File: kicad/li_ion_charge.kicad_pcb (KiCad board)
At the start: 2 copper layers, 17 parts, among them P101 USB_A, P102 CONN_01X02, P103 CONN_01X02, U101 MCP73834-FCI/UN

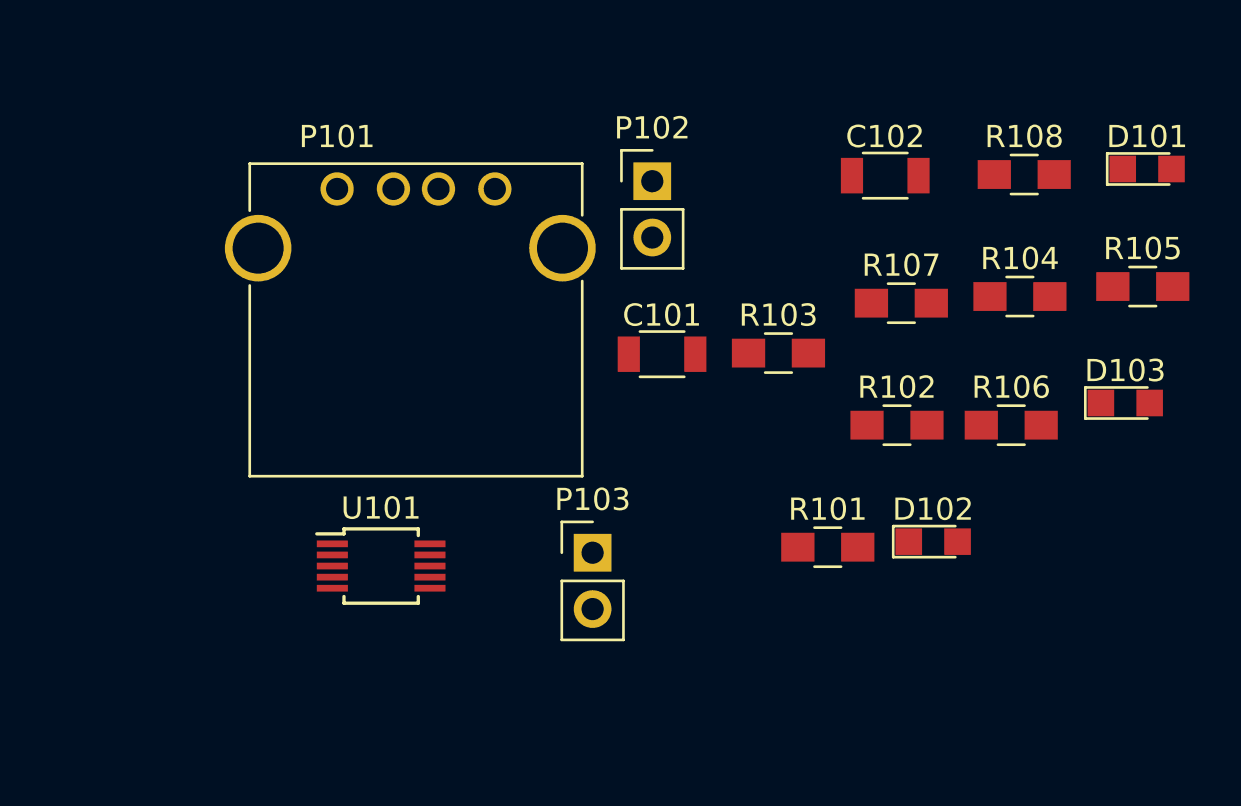
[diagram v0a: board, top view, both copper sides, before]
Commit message: First iteration of complete layout
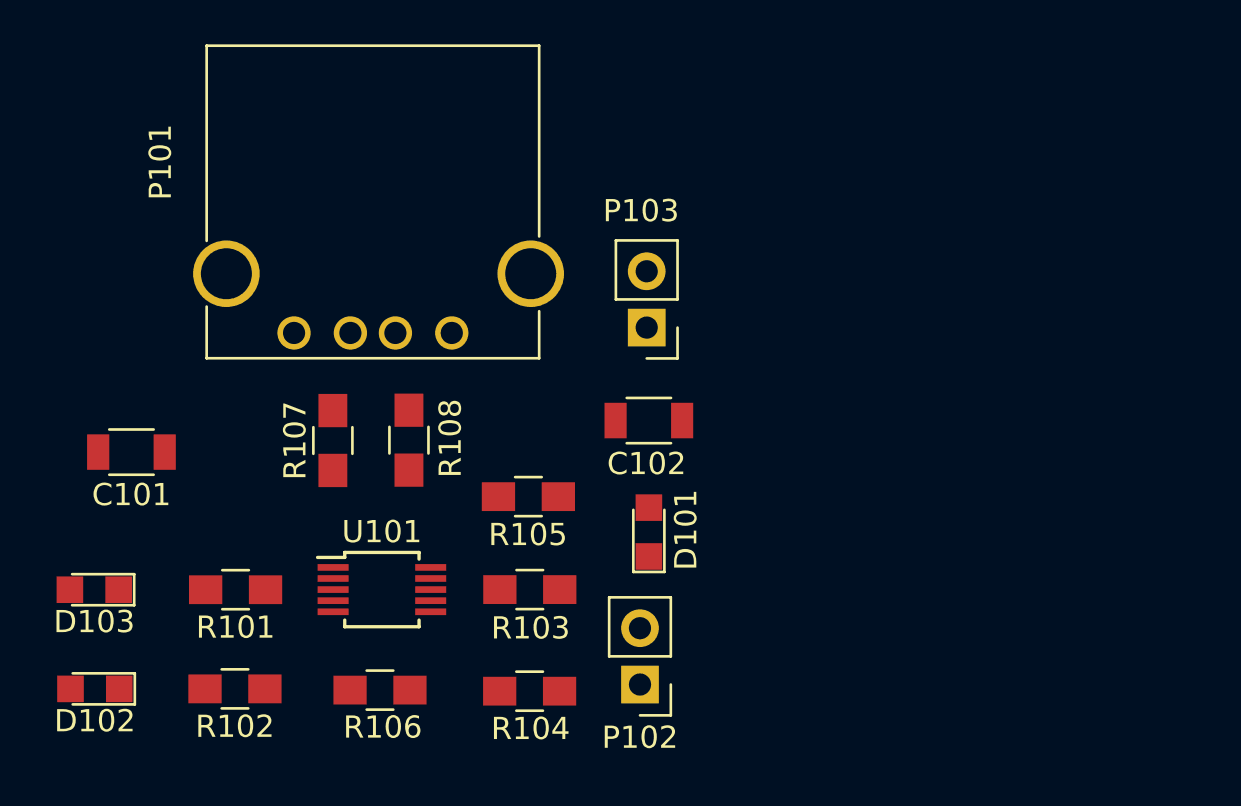
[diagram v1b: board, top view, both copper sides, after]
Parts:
- moved D103 47.2 mm to (145.1, 102.9), turned to 180 degrees
- moved D102 38.4 mm to (145.2, 107.3), turned to 180 degrees
- moved R102 32.1 mm to (151.5, 107.3), turned to 180 degrees
- moved R106 30.9 mm to (158.0, 107.4)
- moved R108 30.2 mm to (159.3, 96.1), turned to 90 degrees
- moved R105 29.3 mm to (164.7, 98.7)
- moved R104 28.4 mm to (164.8, 107.5)
- moved D101 27.8 mm to (170.2, 100.3), turned to 90 degrees
- moved R101 26.8 mm to (151.5, 102.9), turned to 180 degrees
- moved R107 26.4 mm to (155.9, 96.1), turned to 90 degrees
- moved C101 24.3 mm to (146.8, 96.7)
- moved P102 22.7 mm to (169.8, 107.2), turned to 180 degrees
- moved R103 15.5 mm to (164.8, 102.9)
- moved C102 15.3 mm to (170.2, 95.2)
- moved P103 10.4 mm to (170.1, 91.1), turned to 180 degrees
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
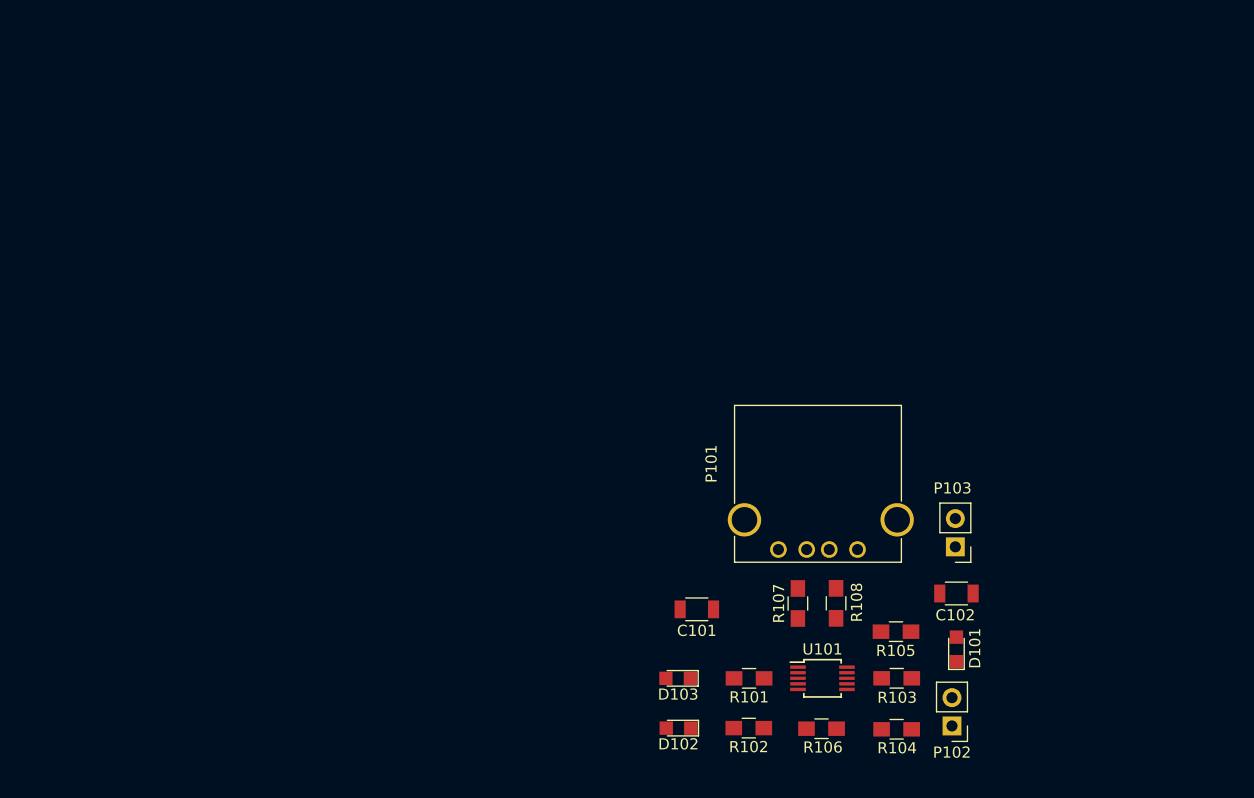
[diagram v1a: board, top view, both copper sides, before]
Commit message: Second iteration of the layout; added several net labels as well
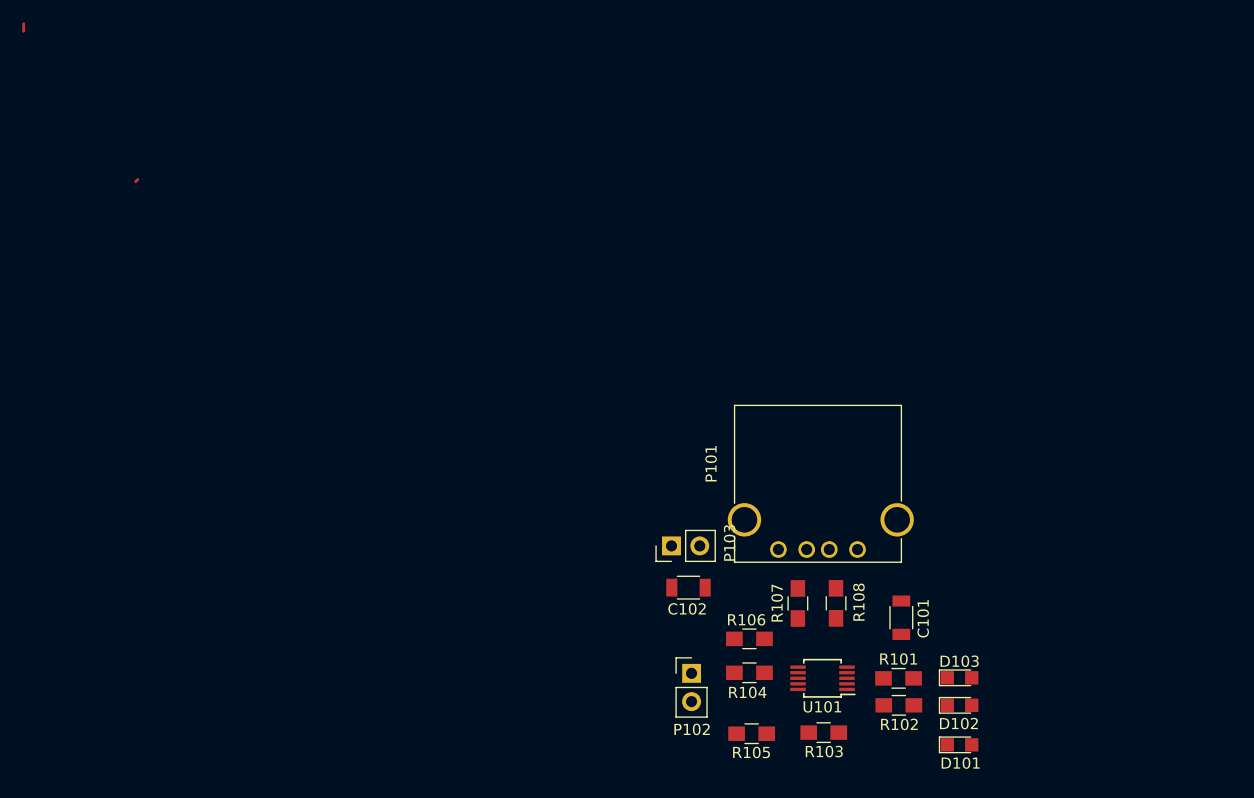
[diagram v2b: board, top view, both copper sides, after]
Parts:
- moved P103 25.5 mm to (144.6, 91.0), turned to 90 degrees
- moved D102 25.3 mm to (170.4, 105.3), turned to 0 degrees
- moved D103 25.3 mm to (170.4, 102.8), turned to 0 degrees
- moved C102 24.1 mm to (146.1, 94.7)
- moved P102 23.9 mm to (146.3, 102.4), turned to 0 degrees
- moved C101 18.4 mm to (165.2, 97.4), turned to 270 degrees
- moved R105 15.9 mm to (151.8, 107.8)
- moved R104 14.2 mm to (151.6, 102.4), turned to 180 degrees
- moved R102 13.6 mm to (165.0, 105.3), turned to 0 degrees
- moved R101 13.4 mm to (164.9, 102.9), turned to 0 degrees
- moved R106 10.4 mm to (151.6, 99.3)
- moved D101 8.58 mm to (170.4, 108.8), turned to 0 degrees
- moved R103 8.17 mm to (158.2, 107.8)
- turned R107 to 270 degrees
- turned R108 to 270 degrees
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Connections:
- net Net-(C101-Pad1) renamed /VIN
- net Net-(C102-Pad1) renamed /VBAT
- net Net-(P102-Pad1) renamed /RESET
- net Net-(R101-Pad1) renamed /Stat1
- net Net-(R102-Pad1) renamed /Stat2
- net Net-(R103-Pad1) renamed /~TE
- net Net-(R105-Pad2) renamed /Ther
- net Net-(R106-Pad2) renamed /Prog
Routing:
- net (no net): track 0.00 -> 0.97 mm

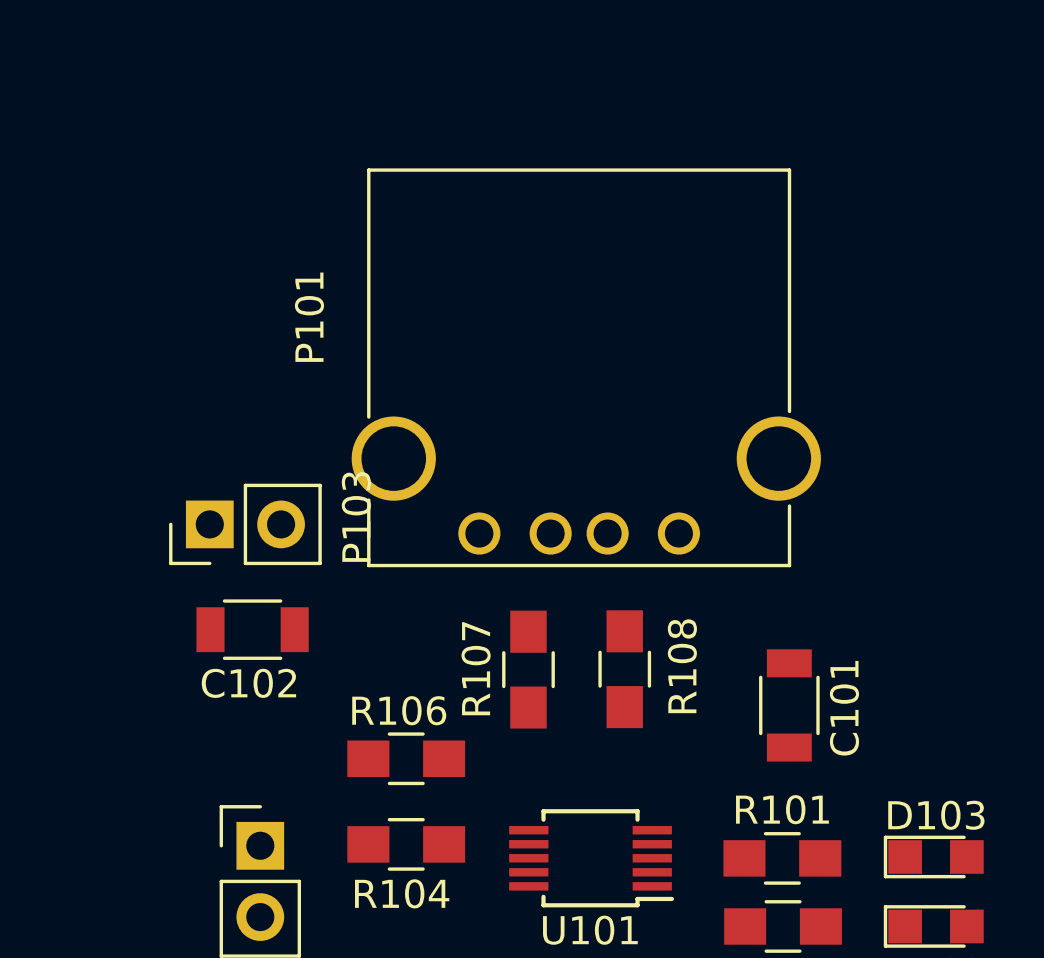
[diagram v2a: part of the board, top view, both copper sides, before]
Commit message: change the schematic to use a micro USB part, and update netlist and layout accordingly
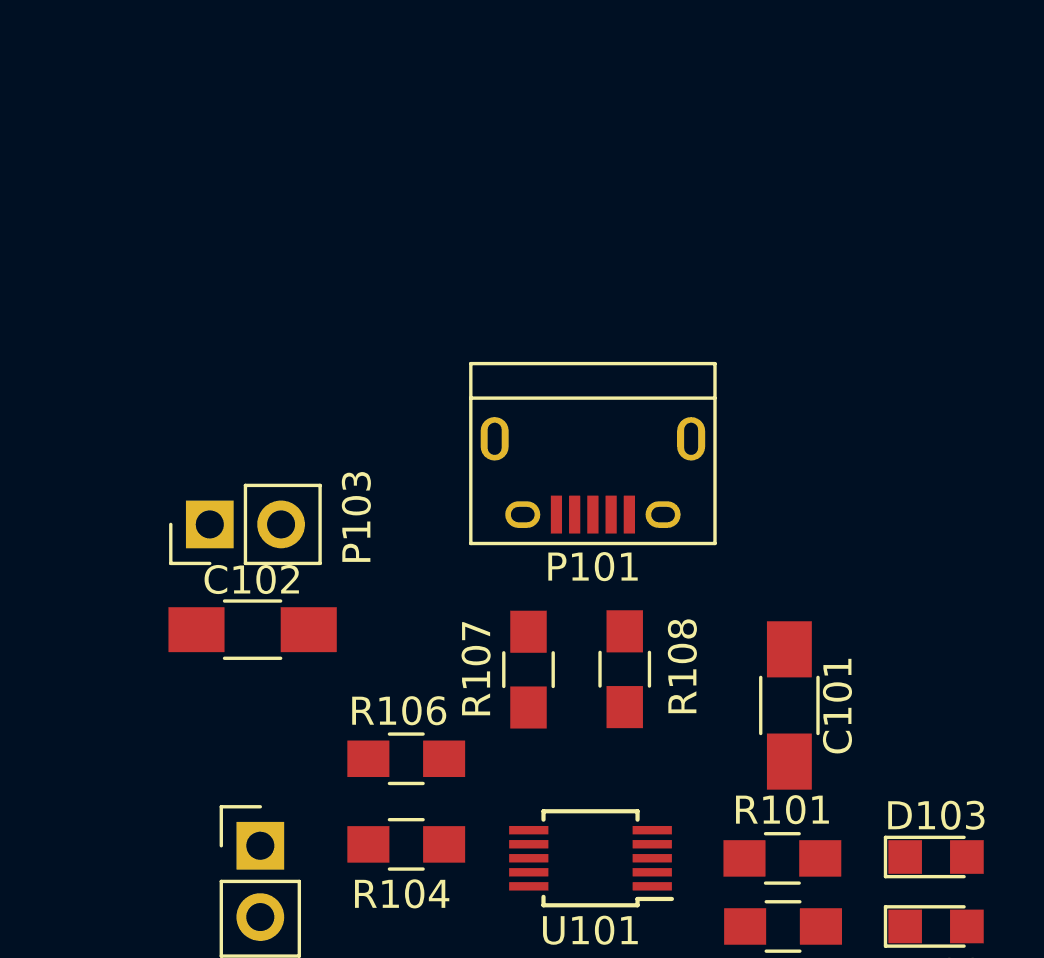
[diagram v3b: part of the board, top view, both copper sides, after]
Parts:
- C101, C102: footprint Capacitors_SMD:C_1206 -> Capacitors_SMD:C_1206_HandSoldering
- P101: value USB_A -> USB_B; footprint Connect:USB_A -> li_ion_charge_library:USB_Micro-B
- moved P101 3.67 mm to (158.2, 89.3)
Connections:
- R107 pad 1: Net-(P101-Pad3) -> GND
- R107 pad 2: GND -> Net-(P101-Pad2)
- R108 pad 1: Net-(P101-Pad2) -> GND
- R108 pad 2: GND -> Net-(P101-Pad3)
